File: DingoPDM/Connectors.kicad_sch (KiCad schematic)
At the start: 11 parts, among them J1 RedCubeTerminal, J2 RedCubeTerminal, J3 Conn_01x12, J5 USB_C_Receptacle_USB2.0

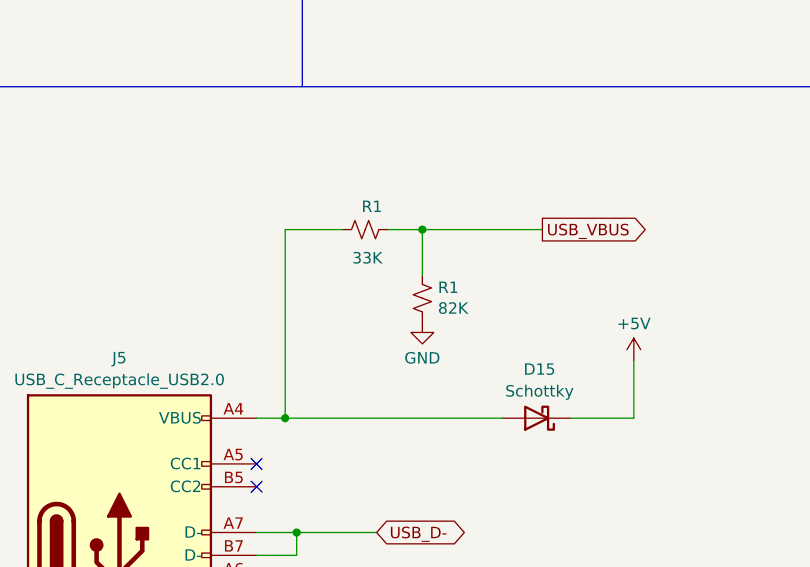
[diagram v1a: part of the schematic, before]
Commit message: Add diode, disconnect PB13, fix USB VBUS
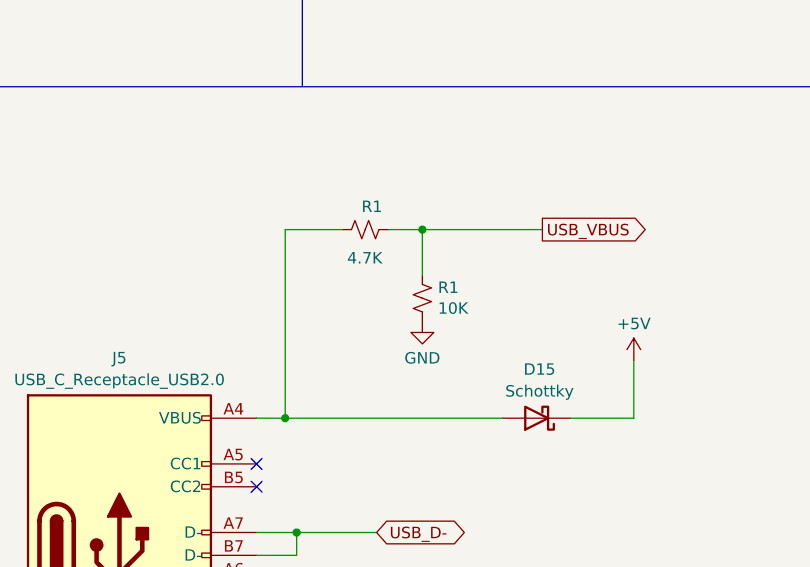
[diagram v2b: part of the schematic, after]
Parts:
- R1: value 82K -> 10K; Digi-Key_PN P82.0KCCT-ND -> 311-10.0KCRDKR-ND; LCSC C212429 -> C17414
- R1: value 33K -> 4.7K; Digi-Key_PN P33.0KCCT-ND -> 311-4.70KCRCT-ND; LCSC C147826 -> C17673
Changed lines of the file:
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@@
   (title_block
     (title "Dingo_PDM")
-    (date "2023-09-04")
-    (rev "v7.1")
+    (date "2023-09-11")
+    (rev "v7.2")
     (comment 3 "github.com/corygrant")
     (comment 4 "Cory Grant")
@@
       (effects (font (size 1.27 1.27)) (justify left))
     )
-    (property "Value" "82K" (at 66.4972 126.238 0)
+    (property "Value" "10K" (at 66.4972 126.238 0)
       (effects (font (size 1.27 1.27)) (justify left))
     )
@@
       (effects (font (size 1.27 1.27)) hide)
     )
-    (property "Digi-Key_PN" "P82.0KCCT-ND" (at 64.77 125.095 0)
-      (effects (font (size 1.27 1.27)) hide)
-    )
-    (property "LCSC" "C212429" (at 64.77 125.095 0)
+    (property "Digi-Key_PN" "311-10.0KCRDKR-ND" (at 64.77 125.095 0)
+      (effects (font (size 1.27 1.27)) hide)
+    )
+    (property "LCSC" "C17414" (at 64.77 125.095 0)
       (effects (font (size 1.27 1.27)) hide)
     )
@@
       (effects (font (size 1.27 1.27)) (justify left))
     )
-    (property "Value" "33K" (at 60.325 120.65 90)
+    (property "Value" "4.7K" (at 60.325 120.65 90)
       (effects (font (size 1.27 1.27)) (justify left))
     )
@@
       (effects (font (size 1.27 1.27)) hide)
     )
-    (property "Digi-Key_PN" "P33.0KCCT-ND" (at 58.42 117.475 0)
-      (effects (font (size 1.27 1.27)) hide)
-    )
-    (property "LCSC" "C147826" (at 58.42 117.475 0)
-      (effects (font (size 1.27 1.27)) hide)
-    )
+    (property "Digi-Key_PN" "311-4.70KCRCT-ND" (at 58.42 117.475 0)
+      (effects (font (size 1.27 1.27)) hide)
+    )
+    (property "LCSC" "C17673" (at 58.42 117.475 0)
+      (effects (font (size 1.27 1.27)) hide)
+    )

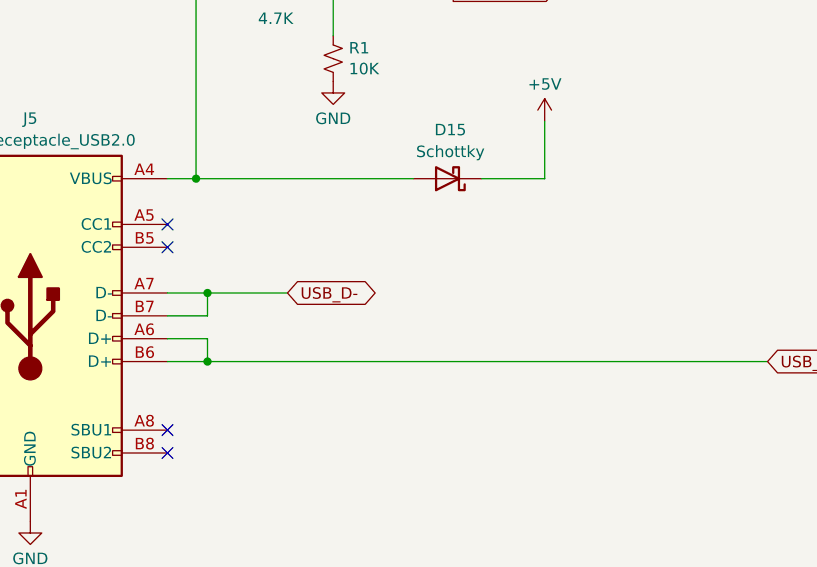
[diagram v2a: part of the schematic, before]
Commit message: Fixed USB, power LED and CAN standby
And increased screw hole size
#9, #11, #12, #13
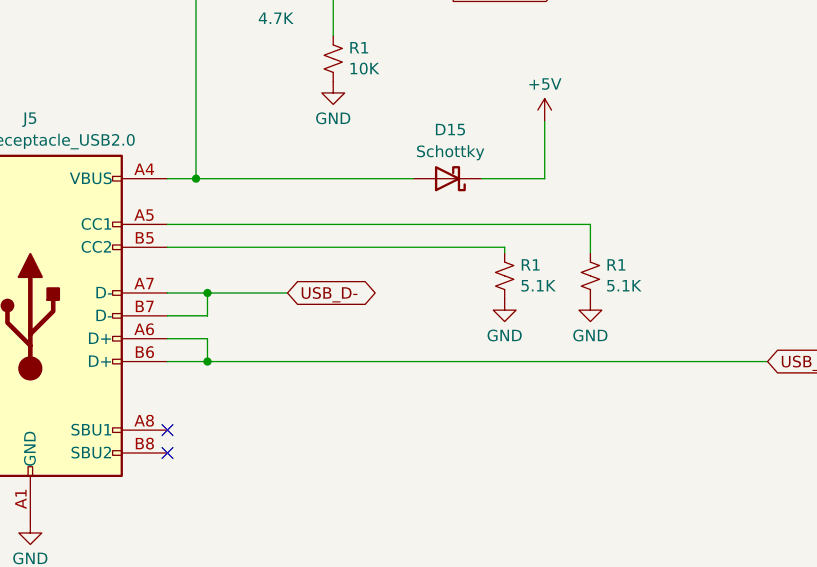
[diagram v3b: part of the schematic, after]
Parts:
- added R1 (x2): 5.1K, Resistor_SMD:R_0805_2012Metric, symbol Device:R_Small_US
- H1, H2, H3, H4: footprint MountingHole:MountingHole_3mm_Pad -> MountingHole:MountingHole_3.2mm_M3_ISO7380_Pad
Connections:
- net GND: now also R1.2, R1.2
- net at J5.A5 (CC1): now also R1.1
- net at J5.B5 (CC2): now also R1.1
- no-connect marks 4 -> 2
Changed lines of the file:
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@@
   (title_block
     (title "Dingo_PDM")
-    (date "2023-09-11")
-    (rev "v7.2")
+    (date "2024-05-26")
+    (rev "v7.3")
     (comment 3 "github.com/corygrant")
     (comment 4 "Cory Grant")
@@
   )
   (no_connect (at 46.355 168.91))
-  (no_connect (at 46.355 143.51))
   (no_connect (at 46.355 166.37))
-  (no_connect (at 46.355 146.05))
   (wire (pts (xy 46.355 153.67) (xy 50.8 153.67))
     (stroke (width 0) (type default))
@@
     (stroke (width 0) (type default))
   )
+  (wire (pts (xy 93.345 143.51) (xy 93.345 146.685))
+    (stroke (width 0) (type default))
+  )
   (polyline (pts (xy 12.065 101.6) (xy 266.065 101.6))
     (stroke (width 0) (type default))
@@
     (stroke (width 0) (type default))
   )
+  (wire (pts (xy 83.82 146.05) (xy 83.82 146.685))
+    (stroke (width 0) (type default))
+  )
   (wire (pts (xy 64.77 117.475) (xy 78.105 117.475))
     (stroke (width 0) (type default))
@@
     (stroke (width 0) (type default))
   )
+  (wire (pts (xy 46.355 146.05) (xy 83.82 146.05))
+    (stroke (width 0) (type default))
+  )
   (wire (pts (xy 50.8 158.75) (xy 113.03 158.75))
     (stroke (width 0) (type default))
@@
   )
   (wire (pts (xy 49.53 117.475) (xy 55.88 117.475))
+    (stroke (width 0) (type default))
+  )
+  (wire (pts (xy 46.355 143.51) (xy 93.345 143.51))
     (stroke (width 0) (type default))
   )
@@
       (effects (font (size 1.27 1.27)) (justify left))
     )
-    (property "Footprint" "MountingHole:MountingHole_3mm_Pad" (at 22.225 73.66 0)
+    (property "Footprint" "MountingHole:MountingHole_3.2mm_M3_ISO7380_Pad" (at 22.225 73.66 0)
       (effects (font (size 1.27 1.27)) hide)
     )
@@
       (effects (font (size 1.27 1.27)) (justify left))
     )
-    (property "Footprint" "MountingHole:MountingHole_3mm_Pad" (at 31.115 73.66 0)
+    (property "Footprint" "MountingHole:MountingHole_3.2mm_M3_ISO7380_Pad" (at 31.115 73.66 0)
       (effects (font (size 1.27 1.27)) hide)
     )
@@
       (effects (font (size 1.27 1.27)) (justify left))
     )
-    (property "Footprint" "MountingHole:MountingHole_3mm_Pad" (at 22.225 78.74 0)
+    (property "Footprint" "MountingHole:MountingHole_3.2mm_M3_ISO7380_Pad" (at 22.225 78.74 0)
       (effects (font (size 1.27 1.27)) hide)
     )
@@
         (path "/8948e307-9174-4227-9c28-3ff885e6e83d/00000000-0000-0000-0000-00005f5b308f"
           (reference "H2") (unit 1)
+        )
+      )
+    )
+  )
+  (symbol (lib_id "Device:R_Small_US") (at 83.82 149.225 0) (unit 1)
+    (in_bom yes) (on_board yes) (dnp no)
+    (property "Reference" "R1" (at 85.5472 148.0566 0)
+      (effects (font (size 1.27 1.27)) (justify left))
+    )
+    (property "Value" "5.1K" (at 85.5472 150.368 0)
+      (effects (font (size 1.27 1.27)) (justify left))
+    )
+    (property "Footprint" "Resistor_SMD:R_0805_2012Metric" (at 83.82 149.225 0)
+      (effects (font (size 1.27 1.27)) hide)
+    )
+    (property "Datasheet" "" (at 83.82 149.225 0)
+      (effects (font (size 1.27 1.27)) hide)
+    )
+    (property "Digi-Key_PN" "311-5.1KARCT-ND" (at 83.82 149.225 0)
+      (effects (font (size 1.27 1.27)) hide)
+    )
+    (property "LCSC" "C218638" (at 83.82 149.225 0)
+      (effects (font (size 1.27 1.27)) hide)
+    )
+    (pin "1")
+    (pin "2")
+    (instances
+      (project "DingoPDM"
+        (path "/8948e307-9174-4227-9c28-3ff885e6e83d"
+          (reference "R1") (unit 1)
+        )
+        (path "/8948e307-9174-4227-9c28-3ff885e6e83d/00000000-0000-0000-0000-00005f5b308f"
+          (reference "R54") (unit 1)
         )
       )
@@
       (effects (font (size 1.27 1.27)) (justify left))
     )
-    (property "Footprint" "MountingHole:MountingHole_3mm_Pad" (at 31.115 78.74 0)
+    (property "Footprint" "MountingHole:MountingHole_3.2mm_M3_ISO7380_Pad" (at 31.115 78.74 0)
       (effects (font (size 1.27 1.27)) hide)
     )
@@
         )
       )
+    )
+  )
+  (symbol (lib_id "Device:R_Small_US") (at 93.345 149.225 0) (unit 1)
+    (in_bom yes) (on_board yes) (dnp no)
+    (property "Reference" "R1" (at 95.0722 148.0566 0)
+      (effects (font (size 1.27 1.27)) (justify left))
+    )
+    (property "Value" "5.1K" (at 95.0722 150.368 0)
+      (effects (font (size 1.27 1.27)) (justify left))
+    )
+    (property "Footprint" "Resistor_SMD:R_0805_2012Metric" (at 93.345 149.225 0)
+      (effects (font (size 1.27 1.27)) hide)
+    )
+    (property "Datasheet" "" (at 93.345 149.225 0)
+      (effects (font (size 1.27 1.27)) hide)
+    )
+    (property "Digi-Key_PN" "311-5.1KARCT-ND" (at 93.345 149.225 0)
+      (effects (font (size 1.27 1.27)) hide)
+    )
+    (property "LCSC" "C218638" (at 93.345 149.225 0)
+      (effects (font (size 1.27 1.27)) hide)
+    )
+    (pin "1")
+    (pin "2")
+    (instances
+      (project "DingoPDM"
+        (path "/8948e307-9174-4227-9c28-3ff885e6e83d"
+          (reference "R1") (unit 1)
+        )
+        (path "/8948e307-9174-4227-9c28-3ff885e6e83d/00000000-0000-0000-0000-00005f5b308f"
+          (reference "R55") (unit 1)
+        )
+      )
+    )
+  )
+  (symbol (lib_name "GND_1") (lib_id "power:GND") (at 93.345 151.765 0) (unit 1)
+    (in_bom yes) (on_board yes) (dnp no) (fields_autoplaced)
+    (property "Reference" "#PWR092" (at 93.345 158.115 0)
+      (effects (font (size 1.27 1.27)) hide)
+    )
+    (property "Value" "GND" (at 93.345 155.8981 0)
+      (effects (font (size 1.27 1.27)))
+    )
+    (property "Footprint" "" (at 93.345 151.765 0)
+      (effects (font (size 1.27 1.27)) hide)
+    )
+    (property "Datasheet" "" (at 93.345 151.765 0)
+      (effects (font (size 1.27 1.27)) hide)
+    )
+    (pin "1")
+    (instances
+      (project "DingoPDM"
+        (path "/8948e307-9174-4227-9c28-3ff885e6e83d/00000000-0000-0000-0000-00005f5b308f"
+          (reference "#PWR092") (unit 1)
+        )
+      )
+    )
+  )
+  (symbol (lib_name "GND_1") (lib_id "power:GND") (at 83.82 151.765 0) (unit 1)
+    (in_bom yes) (on_board yes) (dnp no) (fields_autoplaced)
+    (property "Reference" "#PWR029" (at 83.82 158.115 0)
+      (effects (font (size 1.27 1.27)) hide)
+    )
+    (property "Value" "GND" (at 83.82 155.8981 0)
+      (effects (font (size 1.27 1.27)))
+    )
+    (property "Footprint" "" (at 83.82 151.765 0)
+      (effects (font (size 1.27 1.27)) hide)
+    )
+    (property "Datasheet" "" (at 83.82 151.765 0)
+      (effects (font (size 1.27 1.27)) hide)
+    )
+    (pin "1")
+    (instances
+      (project "DingoPDM"
+        (path "/8948e307-9174-4227-9c28-3ff885e6e83d/00000000-0000-0000-0000-00005f5b308f"
+          (reference "#PWR029") (unit 1)
+        )
+      )

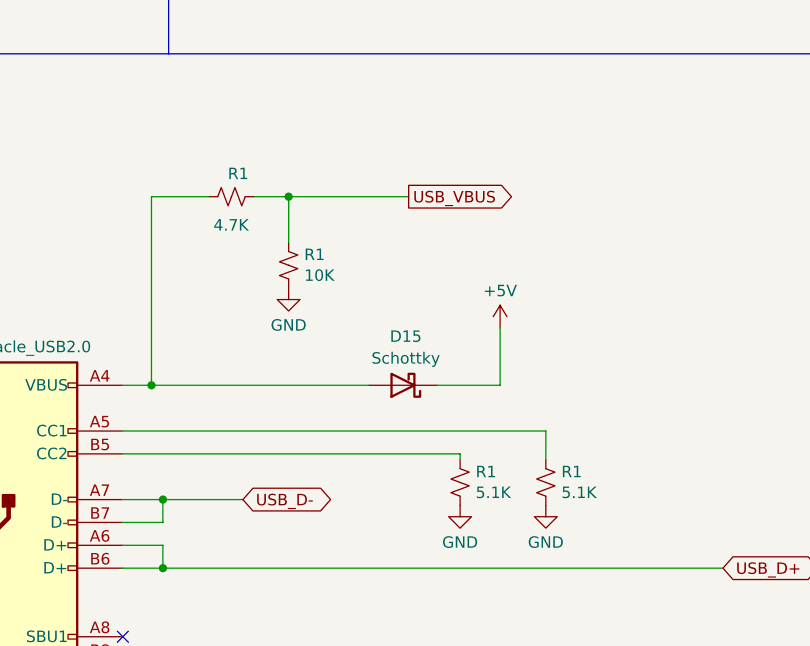
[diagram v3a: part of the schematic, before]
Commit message: Updated to Kicad 8
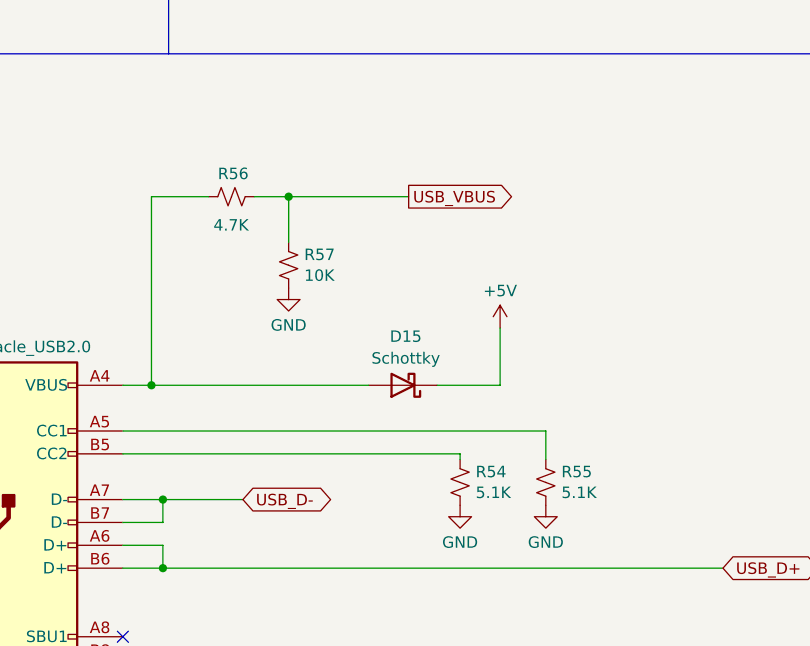
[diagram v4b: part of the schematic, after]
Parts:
- renumbered R1 to R54, R1 to R55, R1 to R56, R1 to R57

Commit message: update to kicad 9.0.1
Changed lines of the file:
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@@
 (kicad_sch
-	(version 20231120)
+	(version 20250114)
 	(generator "eeschema")
-	(generator_version "8.0")
+	(generator_version "9.0")
 	(paper "USLetter")
 	(title_block
@@
 		(comment 3 "github.com/corygrant")
 		(comment 4 "Cory Grant")
+	)
+	(text "1-HIGH\n2-HIGH\n3-MED\n4-MED\n5-MED\n6-MED\n7-MED\n8-MED"
+		(exclude_from_sim no)
+		(at 133.985 62.23 0)
+		(effects
+			(font
+				(size 1.27 1.27)
+			)
+			(justify left bottom)
+		)
+	)
+	(text "Deutsch DT"
+		(exclude_from_sim no)
+		(at 167.005 99.695 0)
+		(effects
+			(font
+				(size 1.27 1.27)
+				(thickness 0.254)
+				(bold yes)
+			)
+			(justify right bottom)
+		)
+	)
+	(text "Battery Lug"
+		(exclude_from_sim no)
+		(at 50.165 52.705 0)
+		(effects
+			(font
+				(size 1.27 1.27)
+				(thickness 0.254)
+				(bold yes)
+			)
+			(justify right bottom)
+		)
+	)
+	(text "Mounting Holes"
+		(exclude_from_sim no)
+		(at 50.165 58.42 0)
+		(effects
+			(font
+				(size 1.27 1.27)
+				(thickness 0.254)
+				(bold yes)
+			)
+			(justify right bottom)
+		)
 	)
 	(junction
@@
 			"+fKIESPmzZu3cOFCJycnCwuLXujt2MuAqVCpVCtXrrx161Z6ejq0gOoWMLqEAQMGAxmmoQ6yCwhO"
 			"f2poaCguLoaOkDqdbubMmQsXLgwICODz+biX0sAA+LU2bdoUFxcXHx/v4+PTLaf9Pw2dsqpV3O3n"
-			"AAAAAElFTkSuQmCC"
-		)
-	)
-	(text "1-HIGH\n2-HIGH\n3-MED\n4-MED\n5-MED\n6-MED\n7-MED\n8-MED"
-		(exclude_from_sim no)
-		(at 133.985 62.23 0)
-		(effects
-			(font
-				(size 1.27 1.27)
-			)
-			(justify left bottom)
-		)
-	)
-	(text "Deutsch DT"
-		(exclude_from_sim no)
-		(at 167.005 99.695 0)
-		(effects
-			(font
-				(size 1.27 1.27)
-				(thickness 0.254)
-				(bold yes)
-			)
-			(justify right bottom)
-		)
-	)
-	(text "Battery Lug"
-		(exclude_from_sim no)
-		(at 50.165 52.705 0)
-		(effects
-			(font
-				(size 1.27 1.27)
-				(thickness 0.254)
-				(bold yes)
-			)
-			(justify right bottom)
-		)
-	)
-	(text "Mounting Holes"
-		(exclude_from_sim no)
-		(at 50.165 58.42 0)
-		(effects
-			(font
-				(size 1.27 1.27)
-				(thickness 0.254)
-				(bold yes)
-			)
-			(justify right bottom)
-		)
-	)
+			"AAAAAElFTkSuQmCCAAAAAAAAAAAAAAAAAAAAAAAAAAAAAAAAAAAAAAAAAAAAAAAAAAAAAAAAAAAA"
+			"AAAAAAAAAAAAAAAAAAAAAAAAAAAAAAAAAAAAAAAAAAAAAAAAAAAAAAAAAAAAAAAAAAAAAAAAAAAA"
+			"AAAAAAAAAAAAAAAAAAAAAAAAAAAAAAAAAAAAAAAAAAAAAAAAAAAAAAAAAAAAAAAAAAAAAAAAAAAA"
+			"AAAAAAAAAAAAAAAAAAAAAAAAAAAAAAAAAAAAAAAAAAAAAAAAAAAAAAAAAAAAAAAAAAAAAAAAAAAA"
+			"AAAAAAAAAAAAAAAAAAAAAAAAAAAAAAAAAAAAAAAAAAAAAAAAAAAAAAAAAAAAAAAAAAAAAAAAAAAA"
+			"AAAAAAAAAAAAAAAAAAAAAAAAAAAAAAAAAAAAAAAAAAAAAAAAAAAAAAAAAAAAAAAAAAAAAAAAAAAA"
+			"AAAAAAAAAAAAAAAAAAAAAAAAAAAAAAAAAAAAAAAAAAAAAAAAAAAAAAAAAAAAAAAAAAAAAAAAAAAA"
+			"AAAAAAAAAAAAAAAAAAAAAAAAAAAAAAAAAAAAAAAAAAAAAAAAAAAAAAAAAAAAAAAAAAAAAAAAAAAA"
+			"AAAAAAAAAAAAAAAAAAAAAAAAAAAAAAAAAAAAAAAAAAAAAAAAAAAAAAAAAAAAAAAAAAAAAAAAAAAA"
+			"AAAAAAAAAAAAAAAAAAAAAAAAAAAAAAAAAAAAAAAAAAAAAAAAAAAAAAAAAAAAAAAAAAAAAAAAAAAA"
+			"AAAAAAAAAAAAAAAAAAAAAAAAAAAAAAAAAAAAAAAAAAAAAAAAAAAAAAAAAAAAAAAAAAAAAAAAAAAA"
+			"AAAAAAAAAAAAAAAAAAAAAAAAAAAAAAAAAAAAAAAAAAAAAAAAAAAAAAAAAAAAAAAAAAAAAAAAAAAA"
+			"AAAAAAAAAAAAAAAAAAAAAAAAAAAAAAAAAAAAAAAAAAAAAAAAAAAAAAAAAAAAAAAAAAAAAAAAAAAA"
+			"AAAAAAAAAAAAAAAAAAAAAAAAAAAAAAAAAAAAAAAAAAAAAAAAAAAAAAAAAAAAAAAAAAAAAAAAAAAA"
+			"AAAAAAAAAAAAAAAAAAAAAAAAAAAAAAAAAAAAAAAAAAAAAAAAAAAAAAAAAAAAAAAAAAAAAAAAAAAA"
+			"AAAAAAAAAAAAAAAAAAAAAAAAAAAAAAAAAAAAAAAAAAAAAAAAAAAAAAAAAAAAAAAAAAAAAAAAAAAA"
+			"AAAAAAAAAAAAAAAAAAAAAAAAAAAAAAAAAAAAAAAAAAAAAAAAAAAAAAAAAAAAAAAAAAAAAAAAAAAA"
+			"AAAAAAAAAAAAAAAAAAAAAAAAAAAAAAAAAAAAAAAAAAAAAAAAAAAAAAAAAAAAAAAAAAAAAAAAAAAA"
+			"AAAAAAAAAAAAAA=="
+		)
+	)
